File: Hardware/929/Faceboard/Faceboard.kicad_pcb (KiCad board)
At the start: 4 copper layers, 154 x 144 mm, 122 parts, among them J1 HDMI, J2 Raspberry_Pi_to_Ziloo, J3 Debug_4-2328724-5, J4 RJ45, J5 UCM-P20-misc, J6 UCM-P21-misc, J7 USB_B_Micro, P1 UCM-P1, P2 UCM-P2, P4 Power, P5 292_PWRCTL-50, P6 292_HIGH-SPEED-50, P7 202-SMART-CAM, Q1 2SC4213, SW1 Reset, SW2 Power, SW3 Alt. Boot, SW4 Power, U1 SN74CB3Q3245RGYR, U10 CBTL04083ABS_518, U11 FSUSB42MUX, U12 Faceboard_Expander_FR2032IG56, U13 LCFE121002H900TG, U14 LCFE121002H900TG, U15 LCFE121002H900TG, U16 TXS0104EPWR, U17 TXS0104EPWR, U18 SN74CB3Q3245RGYR, U19 TXS0104EPWR, U2 SN74CBTLV3126PWR, U20 TXS0104EPWR, U21 TXS0104EPWR, U22 PCA9306DCUR, U23 SN74CB3Q3245RGYR, U3 SN74CB3Q3245RGYR, U4 TPS79618DCQR, U5 LCFE121002H900TG, U6 Supervisor M2 10128793-001RLF, U7 TCA9534, U8 IP4220CZ6, U9 LCFE121002H900TG, Y1 25.000MHz

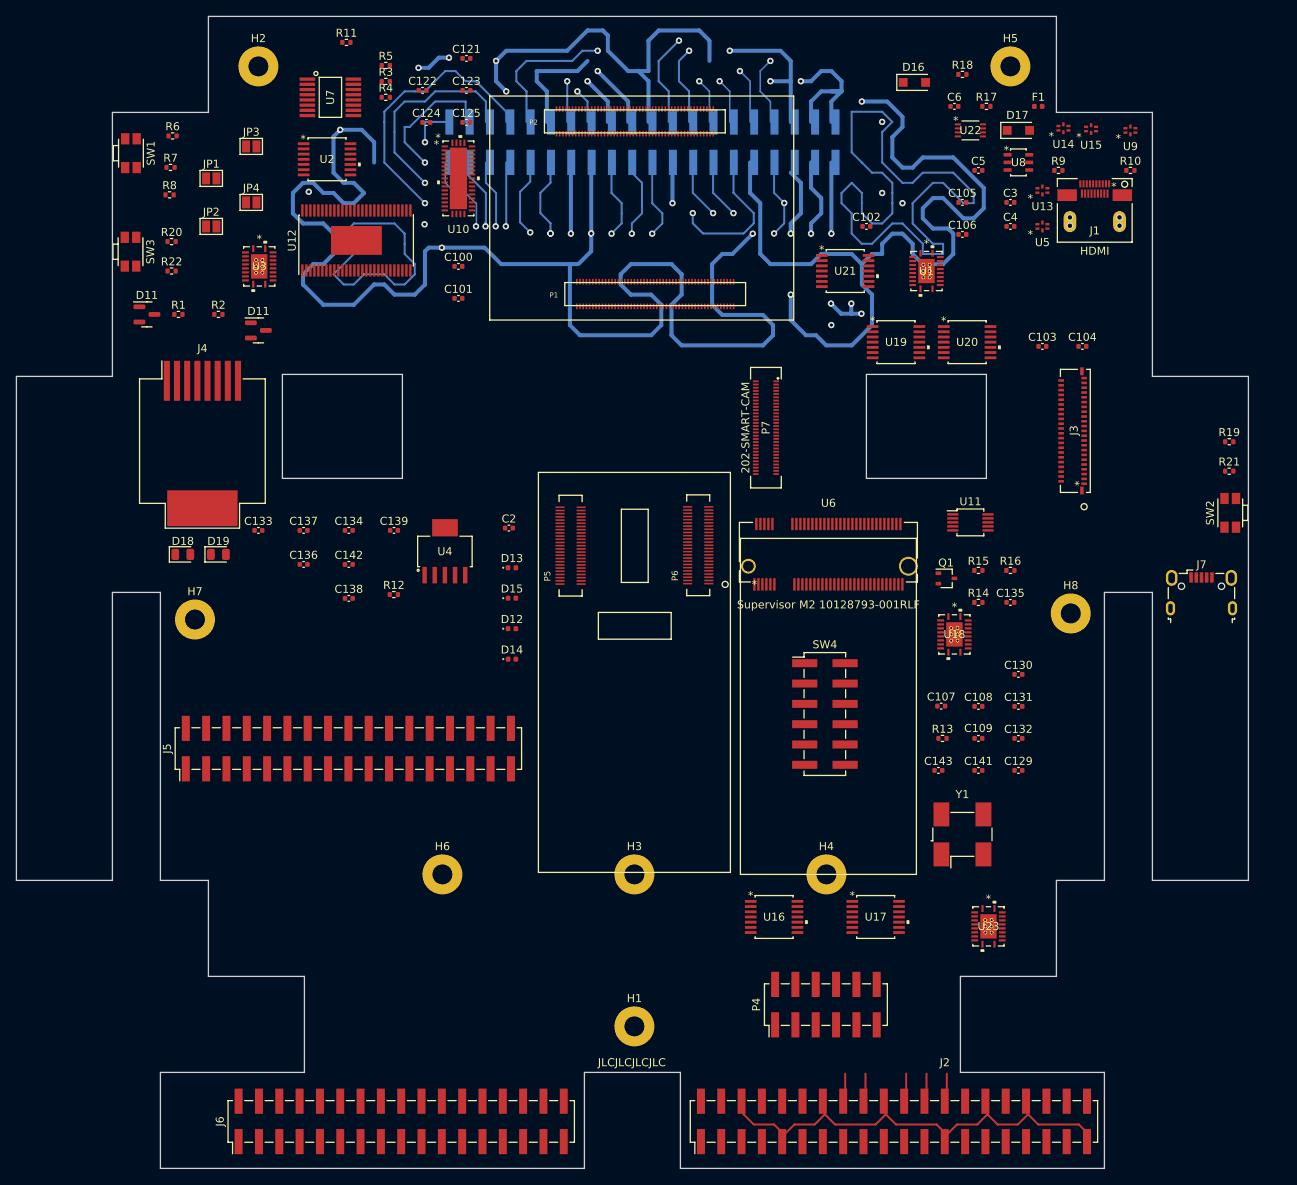
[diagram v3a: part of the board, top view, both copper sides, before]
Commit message: PCB screw holes and rounded corners
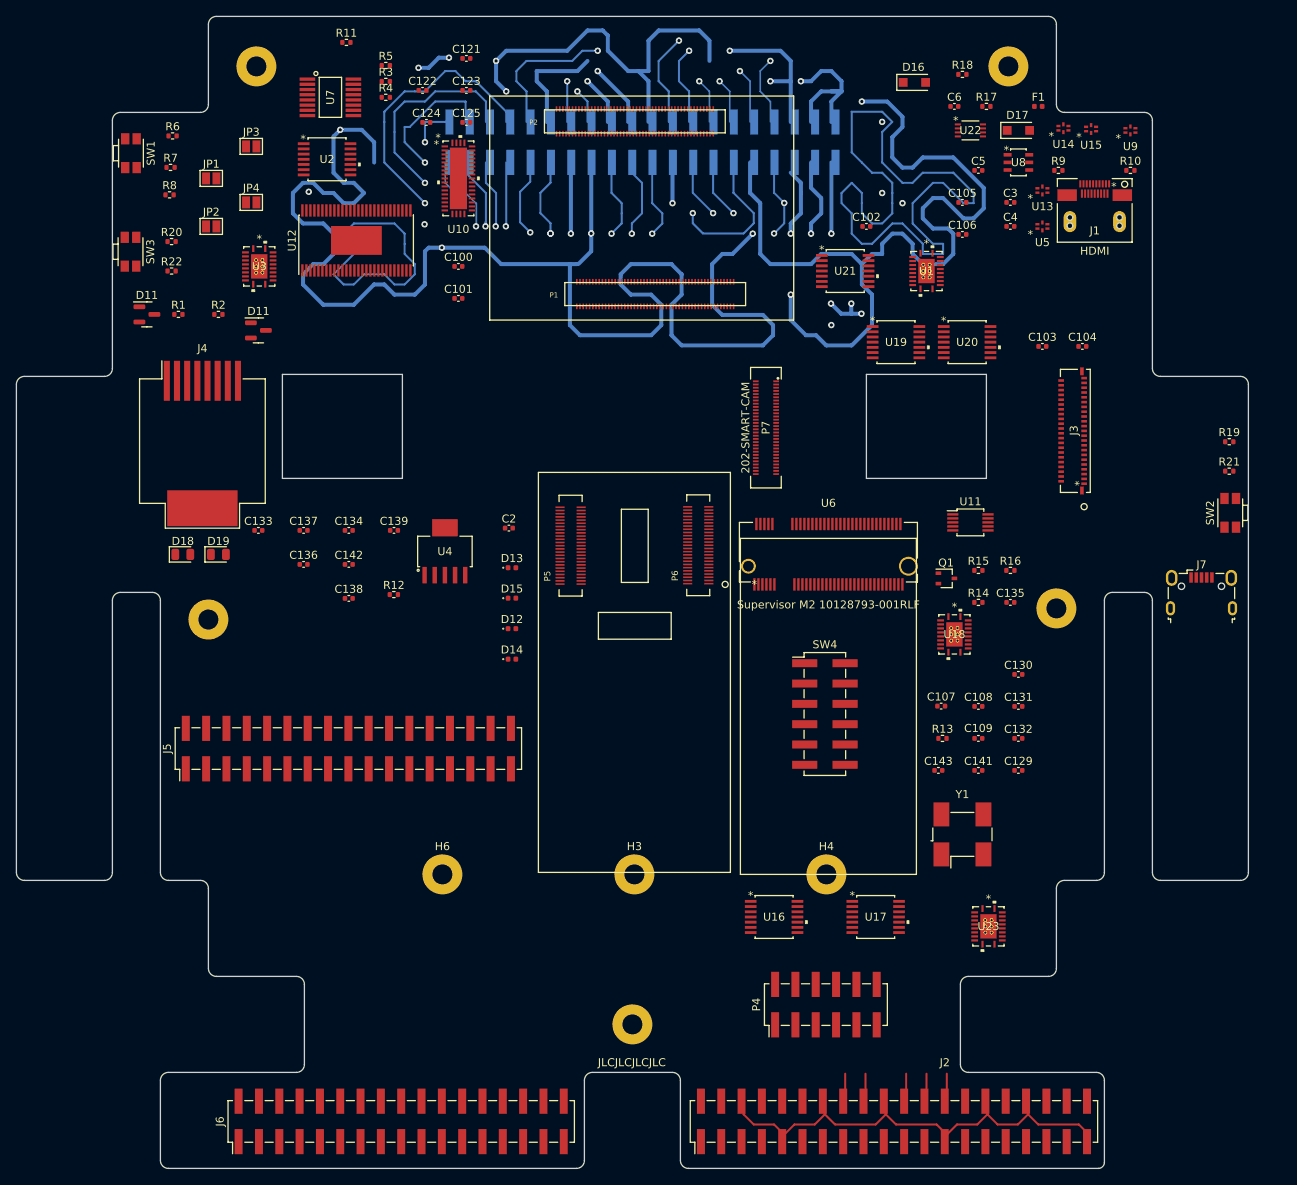
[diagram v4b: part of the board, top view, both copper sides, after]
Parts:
- moved H8 1.90 mm to (160.0, 111.0)
- moved H7 1.68 mm to (54.0, 112.4)
- moved H1 0.35 mm to (107.0, 163.0)
- moved H2 0.25 mm to (60.0, 43.2)
- moved H5 0.25 mm to (154.0, 43.2)
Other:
- outline, holes or cut-outs redrawn
